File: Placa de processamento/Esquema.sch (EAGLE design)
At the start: 11 parts

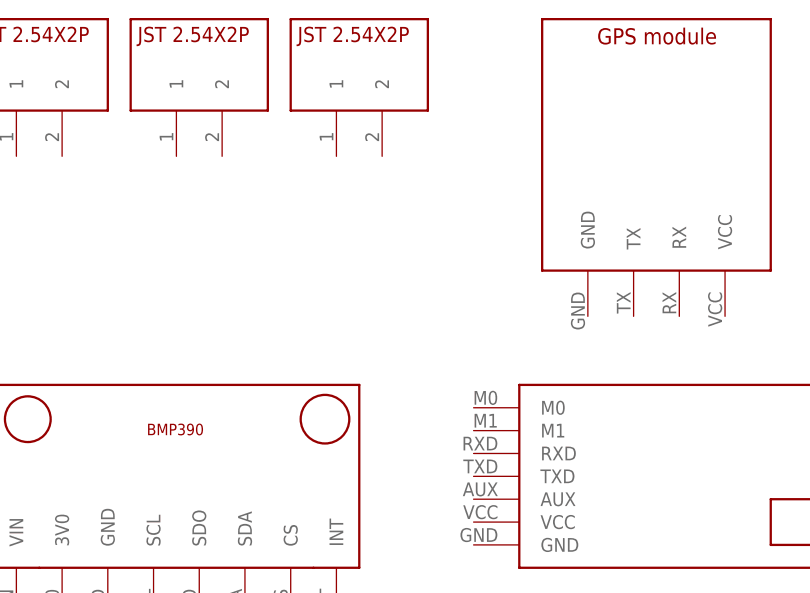
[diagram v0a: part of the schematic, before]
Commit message: Adicionado conexão LoRa
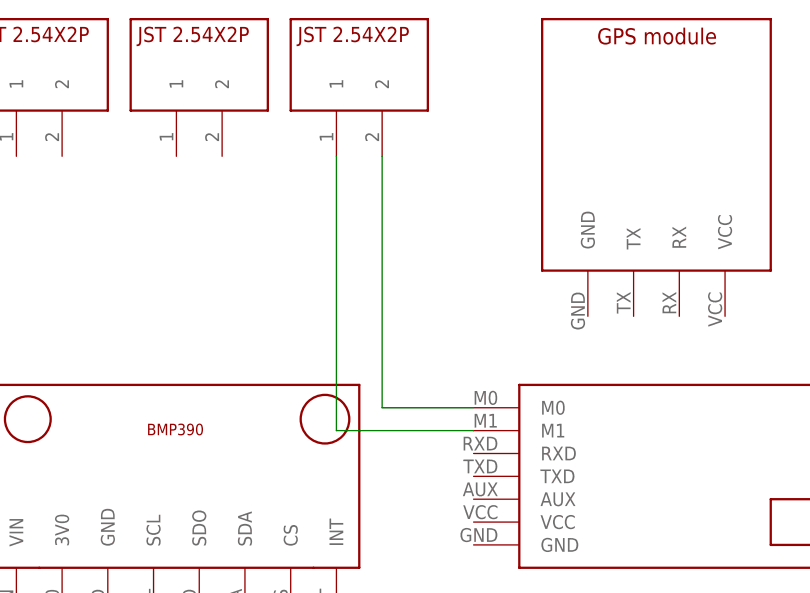
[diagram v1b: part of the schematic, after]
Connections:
- new net N$1: U$2.M0, U$4.2
- new net N$2: U$2.M1, U$4.1
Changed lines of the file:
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@@
 </busses>
 <nets>
+<net name="N$1" class="0">
+<segment>
+<pinref part="U$2" gate="G$1" pin="M0"/>
+<pinref part="U$4" gate="G$1" pin="2"/>
+<wire x1="96.52" y1="43.18" x2="86.36" y2="43.18" width="0.1524" layer="91"/>
+<wire x1="86.36" y1="43.18" x2="86.36" y2="71.12" width="0.1524" layer="91"/>
+</segment>
+</net>
+<net name="N$2" class="0">
+<segment>
+<pinref part="U$2" gate="G$1" pin="M1"/>
+<pinref part="U$4" gate="G$1" pin="1"/>
+<wire x1="96.52" y1="40.64" x2="81.28" y2="40.64" width="0.1524" layer="91"/>
+<wire x1="81.28" y1="40.64" x2="81.28" y2="71.12" width="0.1524" layer="91"/>
+</segment>
+</net>
 </nets>
 </sheet>

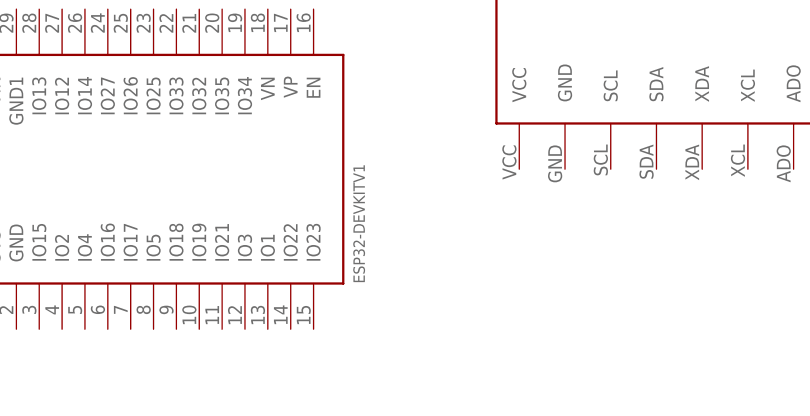
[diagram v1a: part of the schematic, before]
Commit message: Ligado MPU ao ESP32
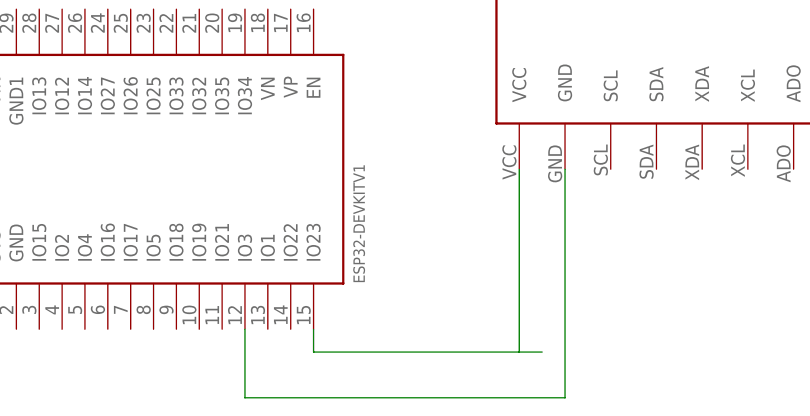
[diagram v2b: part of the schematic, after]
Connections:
- new net N$3: U$11.IO23, U$9.VCC
- new net N$4: U$11.IO3, U$9.GND
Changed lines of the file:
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@@
+</segment>
+</net>
+<net name="N$3" class="0">
+<segment>
+<pinref part="U$9" gate="G$1" pin="VCC"/>
+<wire x1="101.6" y1="-12.7" x2="101.6" y2="-33.02" width="0.1524" layer="91"/>
+<wire x1="101.6" y1="-33.02" x2="104.14" y2="-33.02" width="0.1524" layer="91"/>
+<pinref part="U$11" gate="G$1" pin="IO23"/>
+<wire x1="101.6" y1="-33.02" x2="78.74" y2="-33.02" width="0.1524" layer="91"/>
+<wire x1="78.74" y1="-33.02" x2="78.74" y2="-30.48" width="0.1524" layer="91"/>
+</segment>
+</net>
+<net name="N$4" class="0">
+<segment>
+<pinref part="U$9" gate="G$1" pin="GND"/>
+<wire x1="106.68" y1="-12.7" x2="106.68" y2="-38.1" width="0.1524" layer="91"/>
+<wire x1="106.68" y1="-38.1" x2="71.12" y2="-38.1" width="0.1524" layer="91"/>
+<pinref part="U$11" gate="G$1" pin="IO3"/>
+<wire x1="71.12" y1="-38.1" x2="71.12" y2="-30.48" width="0.1524" layer="91"/>
 </segment>
 </net>

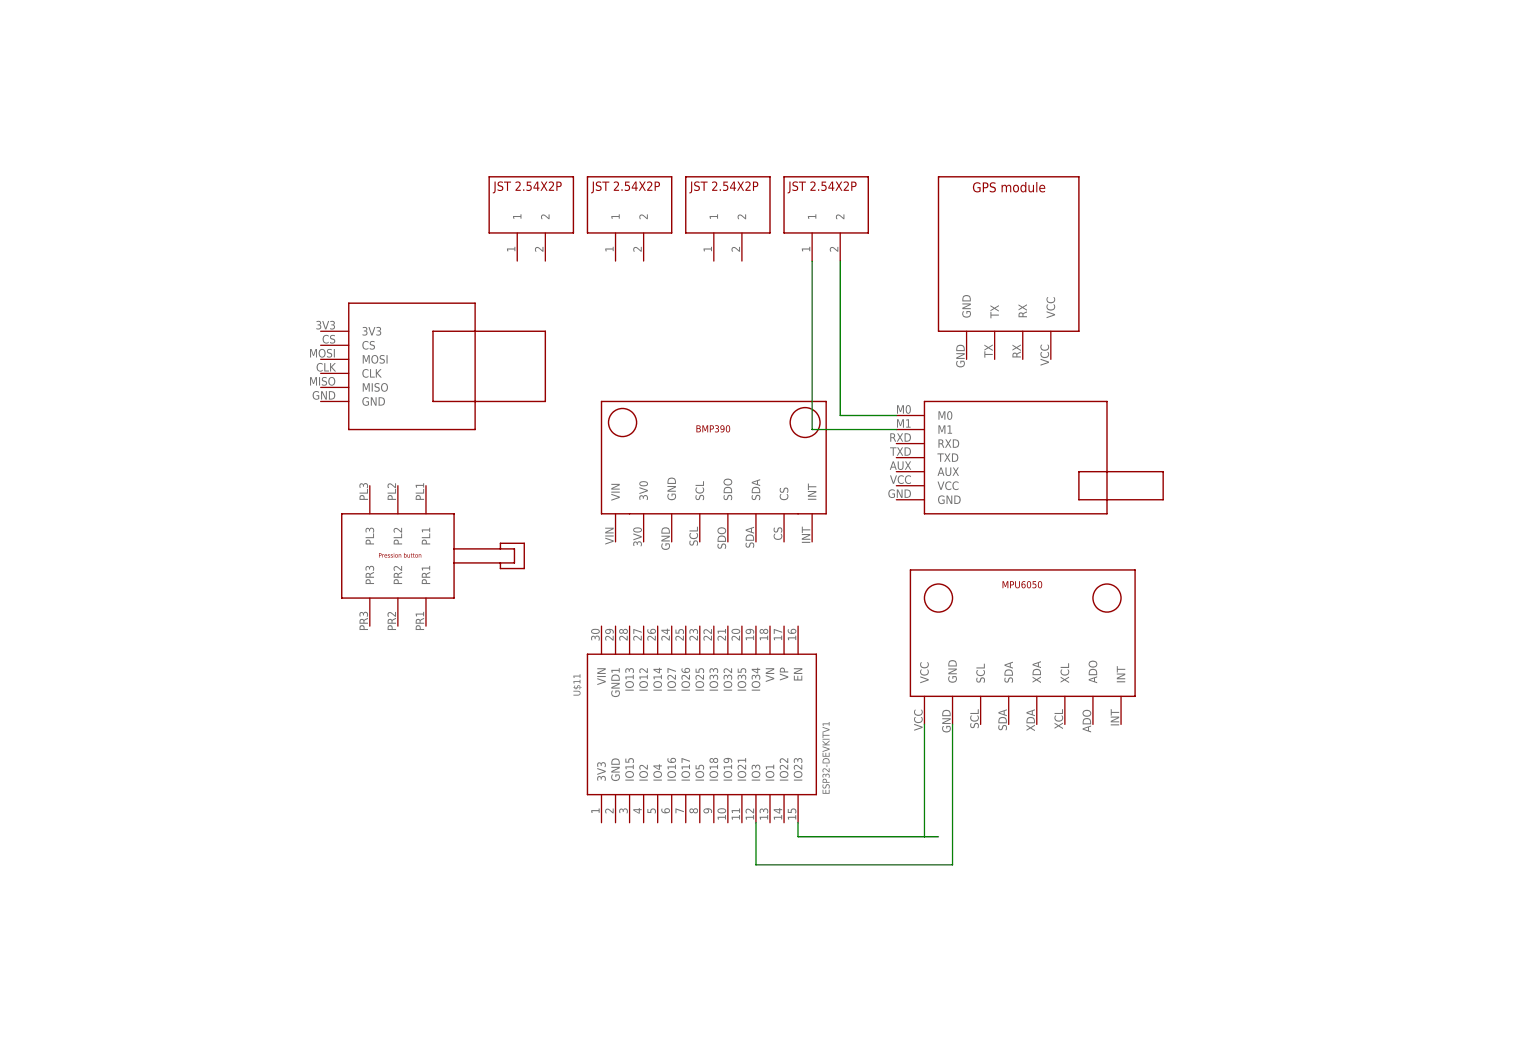
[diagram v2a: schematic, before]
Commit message: Adicionado quase totas as conexões, falta aquelas relacionadas à alimentação (conectores JST)
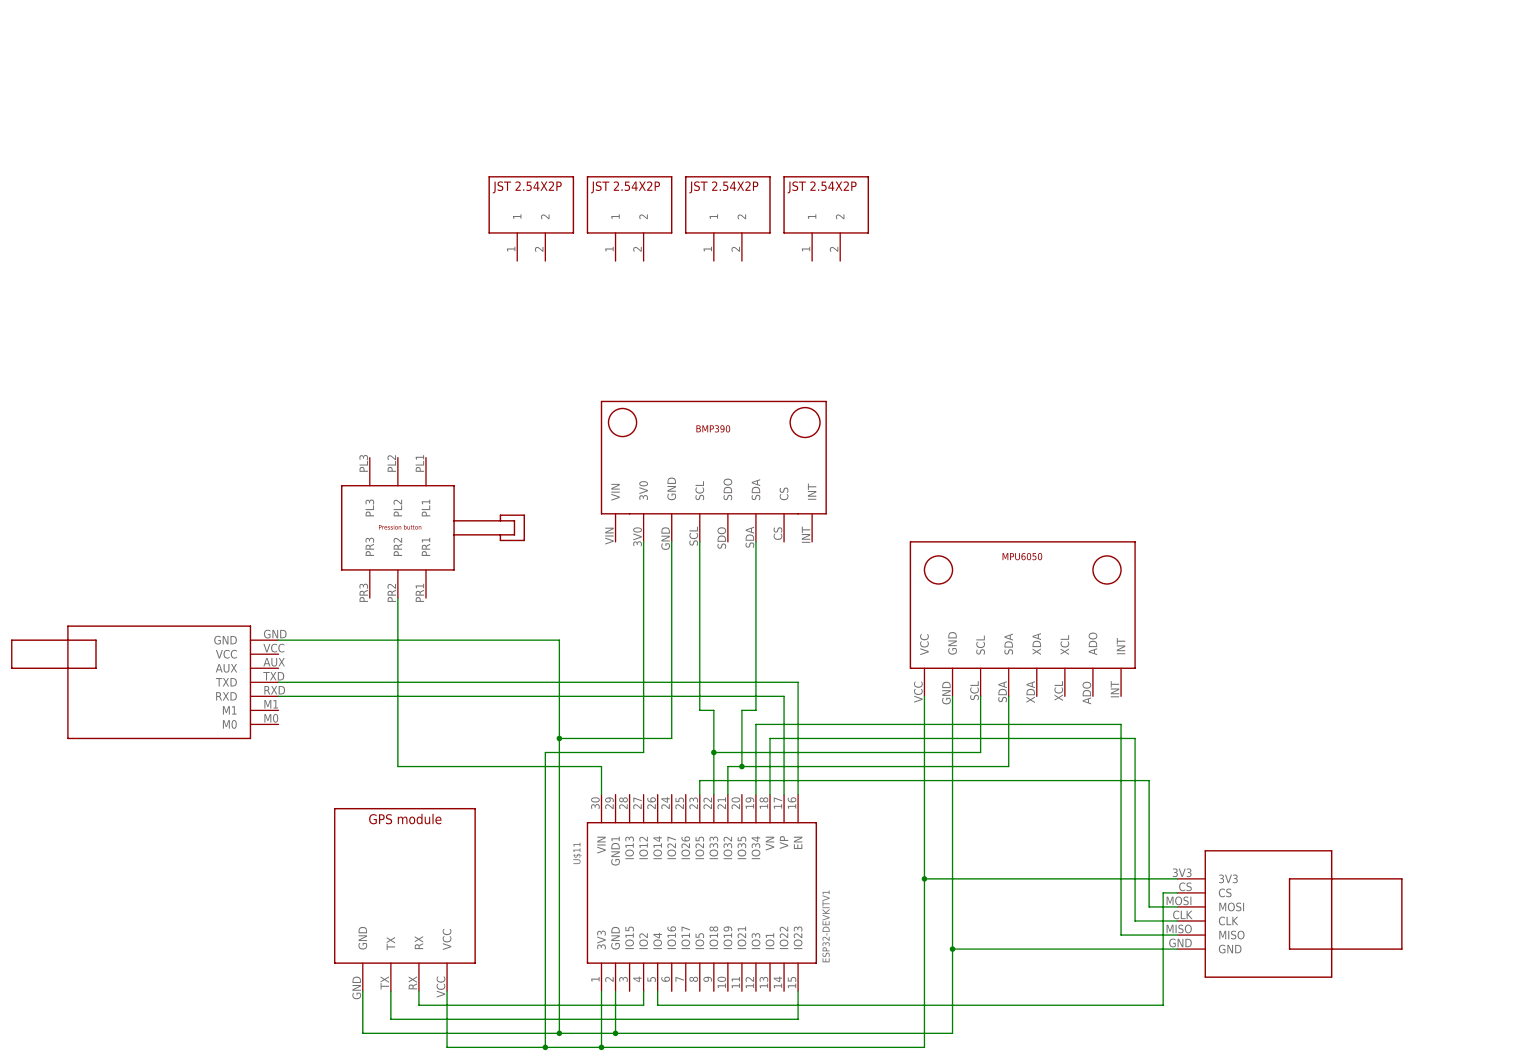
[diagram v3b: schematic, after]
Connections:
- new net N$10: U$11.IO34, U$8.MISO
- new net N$11: U$10.PR2, U$11.VIN
- new net N$13: U$11.VP, U$2.RXD
- new net N$14: U$11.EN, U$2.TXD
- new net N$5: U$11.IO23, U$3.TX
- new net N$6: U$11.IO2, U$3.RX
- new net N$7: U$11.IO4, U$8.CS
- new net N$8: U$11.IO25, U$8.MOSI
- new net N$9: U$11.VN, U$8.CLK
- net N$1: now also U$1.SDA, U$11.IO32, U$9.SDA; no longer U$2.M0, U$4.2
- net N$2: now also U$1.SCL, U$11.IO33, U$9.SCL; no longer U$2.M1, U$4.1
- net N$3: now also U$1.3V0, U$11.3V3, U$3.VCC, U$8.3V3; no longer U$11.IO23
- net N$4: now also U$1.GND, U$11.GND, U$2.GND, U$3.GND, U$8.GND; no longer U$11.IO3
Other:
- moved on the sheet: U$11

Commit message: Roteamento da placa
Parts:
- added IC1: (no value), v-reg:78LXX
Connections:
- new net GND: U$11.GND1, U$7.2
- new net N$12: IC1.OUT, U$2.VCC
- new net N$15: U$11.IO18, U$8.CLK
- new net N$16: U$11.IO19, U$8.MISO
- new net N$19: U$11.IO13, U$6.1
- new net N$20: U$11.IO12, U$6.2
- new net N$21: U$11.IO14, U$4.1
- new net N$22: U$11.IO34, U$5.1
- new net N$23: U$11.IO35, U$5.2
- new net V_BATTERY: U$10.PL3, U$10.PR3, U$7.1
- net N$1: now also U$11.IO21; no longer U$11.IO32
- net N$10: now also U$11.IO33, U$2.M1; no longer U$11.IO34, U$8.MISO
- net N$11: now also U$11.IO32, U$2.M0; no longer U$10.PR2, U$11.VIN
- net N$13: now also U$11.IO5, U$8.CS; no longer U$11.VP, U$2.RXD
- net N$14: now also U$11.IO23, U$8.MOSI; no longer U$11.EN, U$2.TXD
- net N$2: now also U$11.IO22; no longer U$11.IO33
- net N$3: now also U$4.2
- net N$4: now also IC1.GND
- net N$5: now also U$11.IO4, U$3.RX; no longer U$11.IO23, U$3.TX
- net N$6: now also U$11.IO15, U$3.TX; no longer U$11.IO2, U$3.RX
- net N$7: now also IC1.IN, U$10.PL2, U$10.PR2, U$11.VIN; no longer U$11.IO4, U$8.CS
- net N$8: now also U$11.IO17, U$2.TXD; no longer U$11.IO25, U$8.MOSI
- net N$9: now also U$11.IO16, U$2.RXD; no longer U$11.VN, U$8.CLK
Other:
- note added: "12"
- note added: "13"
- note added: "14"
- note added: "3.3v"
- note added: "34"
- note added: "35"
- note added: "Bateria 9v"
- note added: "Buzzer/3.3v"
- note added: "PLACA DE PROCESSAMENTO - JOLIOT"
- note added: "PR3(Botão)"
- note added: "Skibs"
- note added: "gnd"
- note added: "optoaclopadores"
- moved on the sheet: U$11

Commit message: Update
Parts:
- removed IC1: (no value), v-reg:78LXX
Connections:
- removed net GND: U$11.GND1, U$7.2
- removed net N$12: IC1.OUT, U$2.VCC
- removed net N$15: U$11.IO18, U$8.CLK
- removed net N$16: U$11.IO19, U$8.MISO
- removed net N$19: U$11.IO13, U$6.1
- removed net N$20: U$11.IO12, U$6.2
- removed net N$21: U$11.IO14, U$4.1
- removed net N$22: U$11.IO34, U$5.1
- removed net N$23: U$11.IO35, U$5.2
- removed net V_BATTERY: U$10.PL3, U$10.PR3, U$7.1
- net N$1: now also U$11.IO32; no longer U$11.IO21
- net N$10: now also U$11.IO34, U$8.MISO; no longer U$11.IO33, U$2.M1
- net N$11: now also U$10.PR2, U$11.VIN; no longer U$11.IO32, U$2.M0
- net N$13: now also U$11.VP, U$2.RXD; no longer U$11.IO5, U$8.CS
- net N$14: now also U$11.EN, U$2.TXD; no longer U$11.IO23, U$8.MOSI
- net N$2: now also U$11.IO33; no longer U$11.IO22
- net N$3: no longer U$4.2
- net N$4: no longer IC1.GND
- net N$5: now also U$11.IO23, U$3.TX; no longer U$11.IO4, U$3.RX
- net N$6: now also U$11.IO2, U$3.RX; no longer U$11.IO15, U$3.TX
- net N$7: now also U$11.IO4, U$8.CS; no longer IC1.IN, U$10.PL2, U$10.PR2, U$11.VIN
- net N$8: now also U$11.IO25, U$8.MOSI; no longer U$11.IO17, U$2.TXD
- net N$9: now also U$11.VN, U$8.CLK; no longer U$11.IO16, U$2.RXD
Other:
- note removed: "12"
- note removed: "13"
- note removed: "14"
- note removed: "3.3v"
- note removed: "34"
- note removed: "35"
- note removed: "Bateria 9v"
- note removed: "Buzzer/3.3v"
- note removed: "PLACA DE PROCESSAMENTO - JOLIOT"
- note removed: "PR3(Botão)"
- note removed: "Skibs"
- note removed: "gnd"
- note removed: "optoaclopadores"
- moved on the sheet: U$11
